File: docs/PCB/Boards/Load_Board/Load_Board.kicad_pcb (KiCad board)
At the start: 2 copper layers, 128 x 74.8 mm, 180 parts, among them J1 Conn_02x04_Odd_Even, J10 Conn_01x02_Pin, J11 Conn_01x02_Pin, J12 Conn_01x02_Pin, J13 Conn_01x02_Pin, J14 Conn_01x02_Pin, J15 Conn_01x02_Pin, J16 Conn_01x02_Pin, J17 Conn_01x01_Pin, J18 Conn_01x01_Pin, J19 Conn_01x01_Pin, J2 Conn_02x04_Odd_Even, J20 Conn_01x01_Pin, J21 Conn_01x01_Pin, J22 Conn_01x01_Pin, J23 Conn_01x01_Pin, J24 Conn_01x01_Pin, J25 Conn_01x01_Pin, J26 Conn_01x01_Pin, J27 Conn_01x01_Pin, J28 Conn_01x01_Pin, J29 Conn_01x01_Pin, J3 Conn_01x06_Pin, J30 Conn_01x01_Pin, J31 Conn_01x01_Pin, J32 Conn_01x01_Pin, J33 Conn_01x01_Pin, J34 Conn_01x01_Pin, J35 Conn_01x01_Pin, J36 Conn_01x01_Pin, J37 Conn_01x01_Pin, J38 Conn_01x01_Pin, J39 Conn_01x01_Pin, J4 Conn_01x06_Pin, J40 Conn_01x01_Pin, J41 Conn_01x01_Pin, J42 Conn_01x01_Pin, J43 Conn_01x01_Pin, J44 Conn_01x01_Pin, J45 Conn_01x01_Pin, J46 Conn_01x01_Pin, J47 Conn_01x01_Pin, J48 Conn_01x01_Pin, J49 Conn_01x01_Pin, J5 Conn_01x02_Pin, J50 Conn_01x01_Pin, J51 Conn_01x01_Pin, J52 Conn_01x01_Pin, J53 Conn_01x01_Pin, J54 Conn_01x01_Pin, J55 Conn_01x01_Pin, J56 Conn_01x01_Pin, J57 Conn_01x01_Pin, J58 Conn_01x01_Pin, J59 Conn_01x01_Pin, J6 Conn_01x02_Pin, J60 Conn_01x01_Pin, J61 Conn_01x01_Pin, J62 Conn_01x01_Pin, J63 Conn_01x01_Pin, J64 Conn_01x01_Pin, J65 Conn_01x01_Pin, J66 Conn_01x01_Pin, J67 Conn_01x01_Pin, J68 Conn_01x01_Pin, J69 Conn_01x01_Pin, J7 Conn_01x02_Pin, J70 Conn_01x01_Pin, J71 Conn_01x01_Pin, J72 Conn_01x01_Pin, J73 Conn_01x01_Pin, J74 Conn_01x01_Pin, J75 Conn_01x01_Pin, J76 Conn_01x01_Pin, J77 Conn_01x01_Pin, J78 Conn_01x01_Pin, J79 Conn_01x01_Pin, J8 Conn_01x02_Pin, J80 Conn_01x01_Pin, J81 Conn_01x01_Pin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

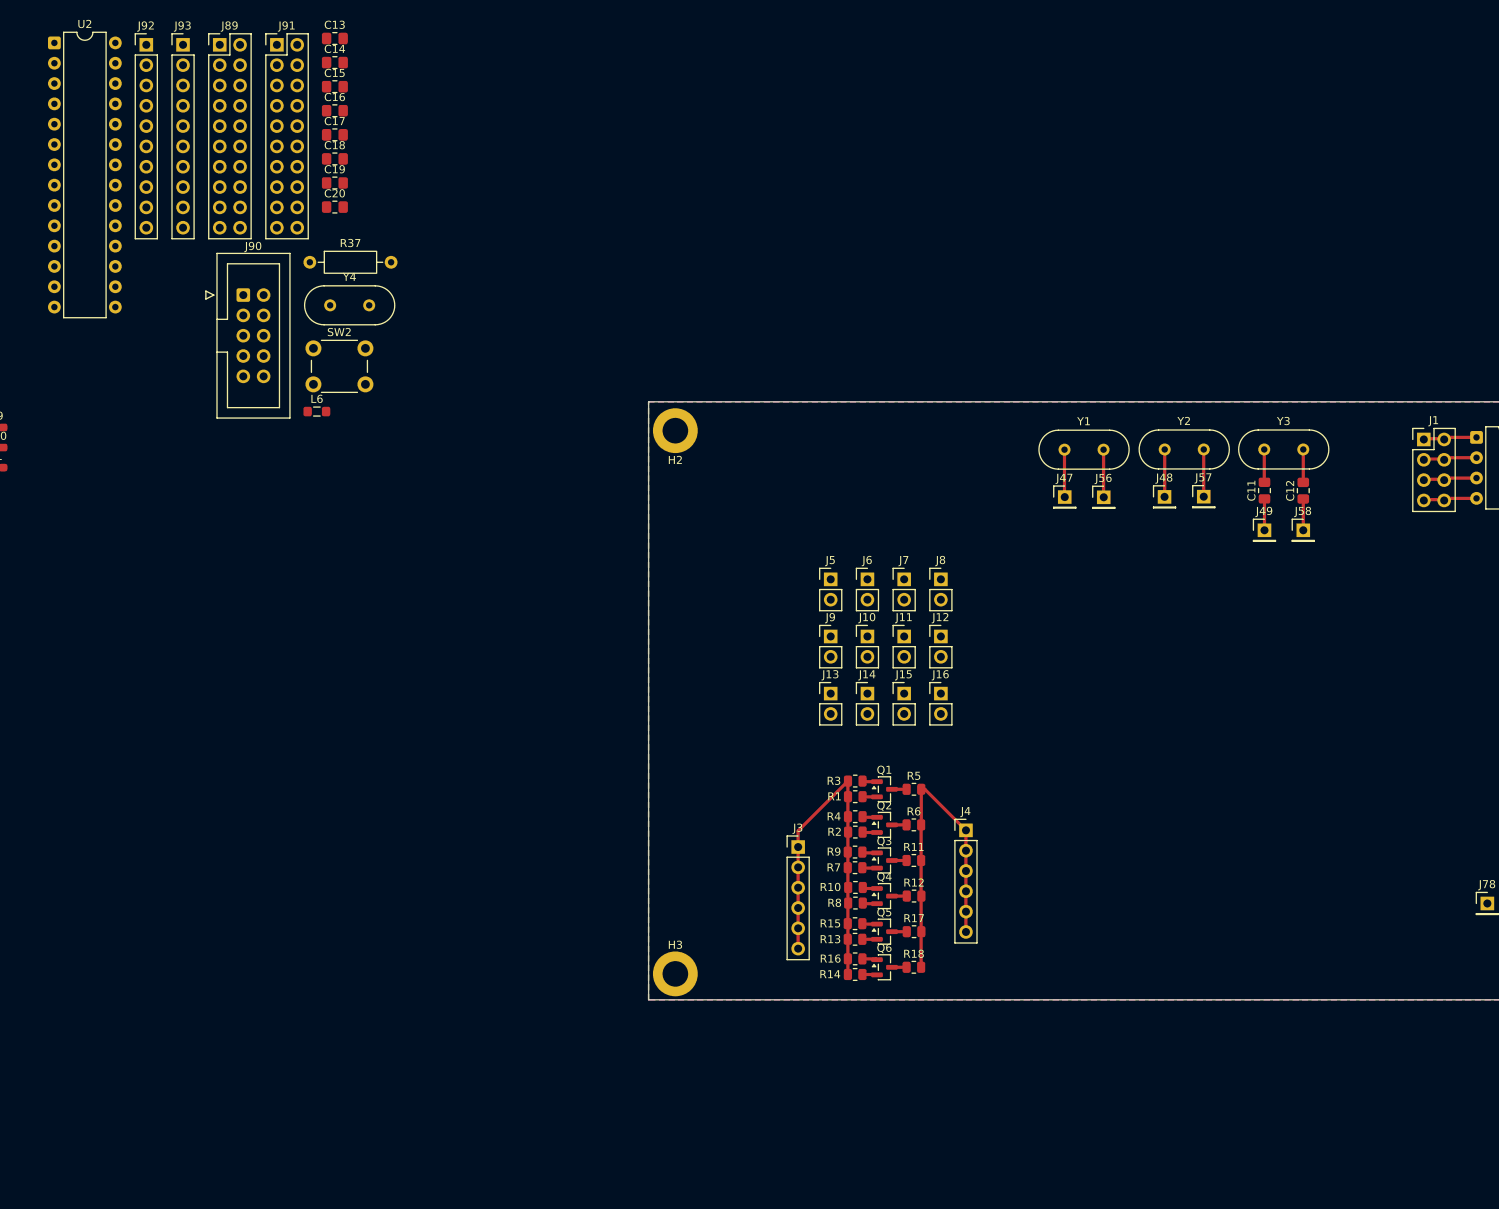
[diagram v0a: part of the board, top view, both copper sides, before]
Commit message: Load Board updated.
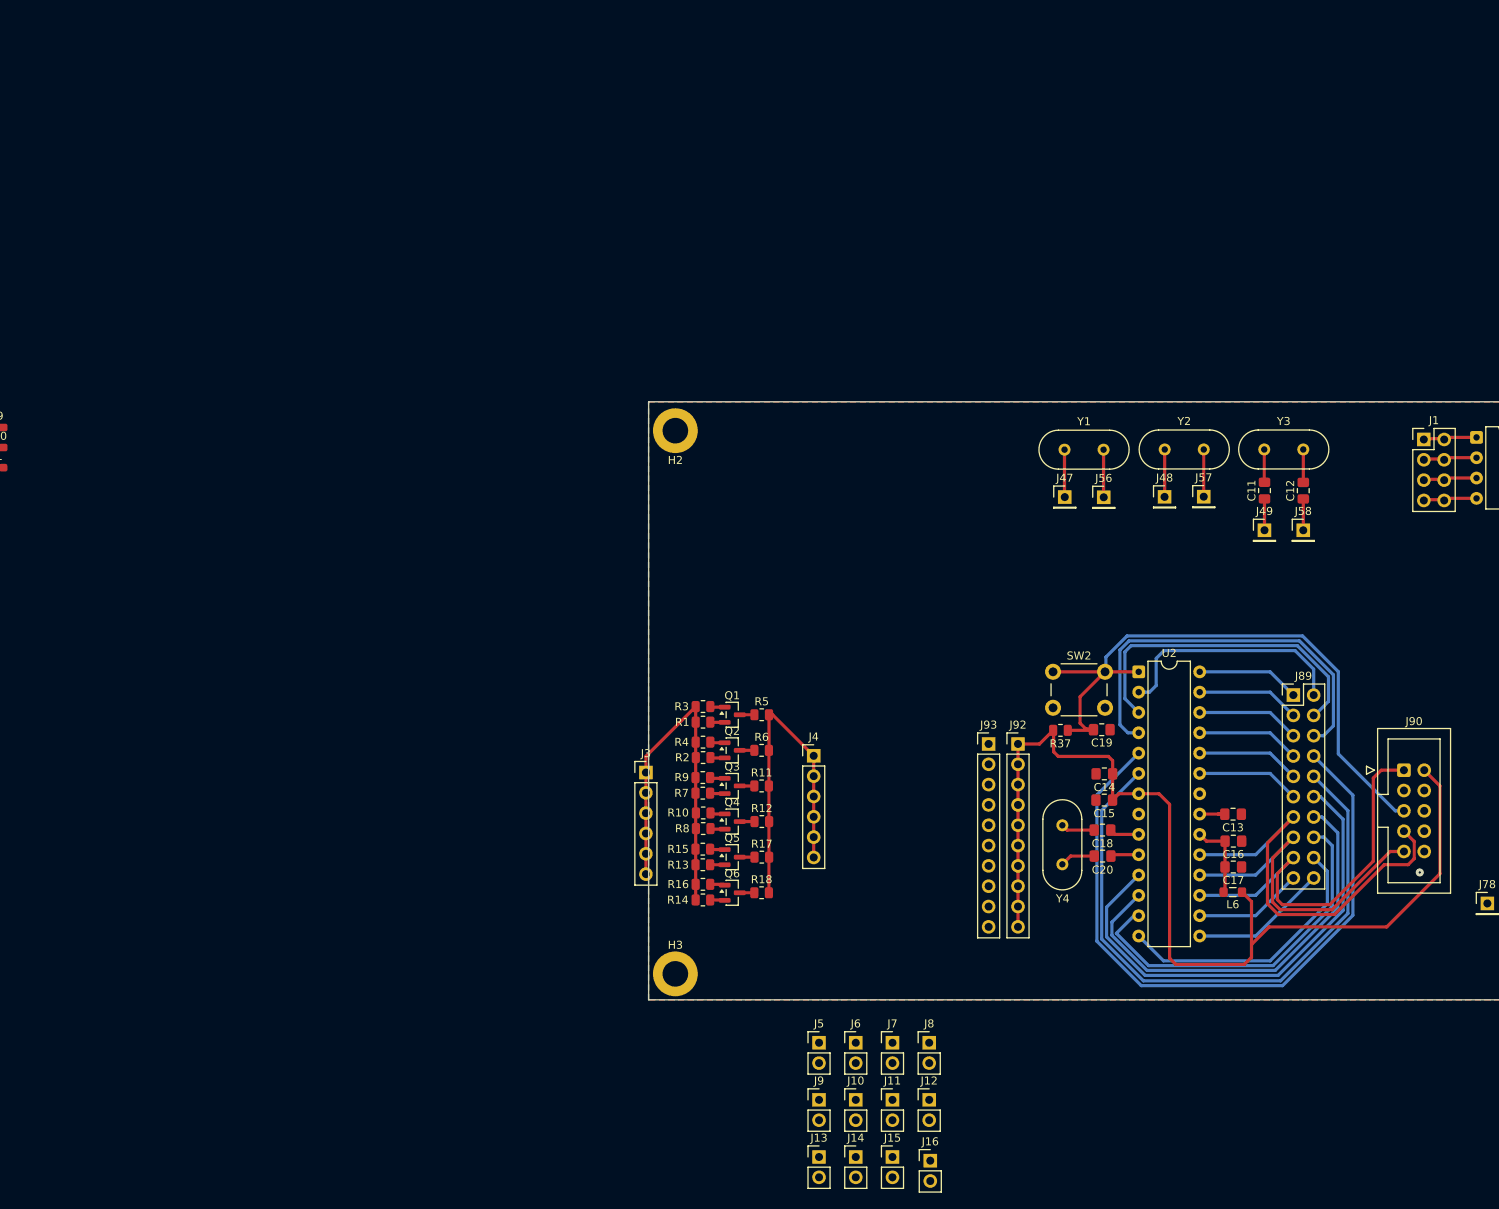
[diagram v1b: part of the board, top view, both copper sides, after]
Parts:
- removed J91: Conn_02x10_Odd_Even, Connector_PinHeader_2.54mm:PinHeader_2x10_P2.54mm_Vertical
- J90: value AVR-ISP-6 -> AVR-ISP-10
- R37: footprint Resistor_THT:R_Axial_DIN0207_L6.3mm_D2.5mm_P10.16mm_Horizontal -> Resistor_SMD:R_0805_2012Metric
- moved J89 156.9 mm to (202.3, 94.1)
- moved J90 156.8 mm to (216.1, 103.5)
- moved U2 156.7 mm to (183.0, 91.2)
- moved C13 148.3 mm to (194.8, 109.0), turned to 180 degrees
- moved C17 144.9 mm to (194.8, 115.6)
- moved C16 144.7 mm to (194.8, 112.4)
- moved J92 139.7 mm to (167.9, 100.2)
- moved J93 133.3 mm to (164.2, 100.2)
- moved C15 131.2 mm to (178.7, 107.2)
- moved C14 131.0 mm to (178.7, 104.0)
- moved L6 129.3 mm to (194.7, 118.7), turned to 180 degrees
- moved C18 127.5 mm to (178.4, 111.0), turned to 180 degrees
- moved C20 125.7 mm to (178.4, 114.2)
- moved C19 117.7 mm to (178.3, 98.4)
- moved Y4 112.3 mm to (173.4, 110.4), turned to -90 degrees
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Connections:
- J89 pad 1: PB0 -> PC5
- J89 pad 10: PD2 -> PD4
- J89 pad 11: PB5 -> PC0
- J89 pad 12: PD3 -> PD5
- J89 pad 13: PC0 -> PB5
- J89 pad 14: PD4 -> PD6
- J89 pad 15: PC1 -> PB4
- J89 pad 16: PD5 -> PD7
- J89 pad 17: PC2 -> PB3
- J89 pad 18: PD6 -> PB0
- J89 pad 19: PC3 -> PB2
- J89 pad 2: PC4 -> PD0
- J89 pad 20: PD7 -> PB1
- J89 pad 3: PB1 -> PC4
- J89 pad 4: PC5 -> PD1
- J89 pad 5: PB2 -> PC3
- J89 pad 6: PD0 -> PD2
- J89 pad 7: PB3 -> PC2
- J89 pad 8: PD1 -> PD3
- J89 pad 9: PB4 -> PC1
- J90 pad 1: PB4 -> PB3
- J90 pad 10: (no net) -> GND
- J90 pad 3: PB5 -> unconnected-(J90-NC-Pad3)
- J90 pad 4: PB3 -> GND
- J90 pad 7: (no net) -> PB5
- J90 pad 8: (no net) -> GND
- J90 pad 9: (no net) -> PB4
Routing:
- net 5V: track 0.00 -> 131.2 mm
- net PD3: track 0.00 -> 85.6 mm
- net RESET: track 0.00 -> 79.2 mm
- net PD4: track 0.00 -> 78.0 mm
- net PD5: track 0.00 -> 60.6 mm
- net PD6: track 0.00 -> 52.9 mm
- net PB5: track 0.00 -> 51.6 mm
- net PD2: track 0.00 -> 50.4 mm
- net PB3: track 0.00 -> 48.9 mm
- net PD7: track 0.00 -> 45.8 mm
- net PB4: track 0.00 -> 42.7 mm
- net PD1: track 0.00 -> 41.3 mm
- net PB0: track 0.00 -> 34.3 mm
- net PD0: track 0.00 -> 31.0 mm
- net PB1: track 0.00 -> 17.3 mm
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
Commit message: Load board and ATMega Board added
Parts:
- removed C13, C14, C16, C19: 100nF, Capacitor_SMD:C_0805_2012Metric_Pad1.18x1.45mm_HandSolder
- removed C15, C17: 1uF, Capacitor_SMD:C_0805_2012Metric_Pad1.18x1.45mm_HandSolder
- removed C18, C20: 22pF, Capacitor_SMD:C_0805_2012Metric_Pad1.18x1.45mm_HandSolder
- removed J17, J18, J19, J20, J39, J40, J41, J42, J43, J44, J45, J46, J47, J48, J49, J50, J51, J52, J53, J54, J55, J56, J57, J58, J59, J60, J61, J62, J63, J64, J65, J66, J67, J68, J69, J70, J71, J72, J73, J74, J75, J76, J77, J78, J79, J80, J81, J82, J83, J84, J85, J86, J87, J88: Conn_01x01_Pin, Connector_PinHeader_2.54mm:PinHeader_1x01_P2.54mm_Vertical
- removed J89: Conn_02x10_Odd_Even, Connector_PinHeader_2.54mm:PinHeader_2x10_P2.54mm_Vertical
- removed J90: AVR-ISP-10, Connector_IDC:IDC-Header_2x05_P2.54mm_Vertical
- removed J92, J93: Conn_01x10_Pin, Connector_PinHeader_2.54mm:PinHeader_1x10_P2.54mm_Vertical
- removed L6: 600 Ω@100 MHz, Inductor_SMD:L_0805_2012Metric_Pad1.05x1.20mm_HandSolder
- removed R37: 1K, Resistor_SMD:R_0805_2012Metric
- removed SW2: Tact Switch 6x6mm / 13mm, Button_Switch_THT:SW_PUSH_6mm
- removed U2: ATmega328P-P, Package_DIP:DIP-28_W7.62mm
- removed Y4: Crystal, Crystal:Crystal_HC49-4H_Vertical
- J10: value Conn_01x02_Pin -> LVL_OUT_3; footprint Connector_PinHeader_2.54mm:PinHeader_1x02_P2.54mm_Vertical -> Connector_PinHeader_2.54mm:PinHeader_1x01_P2.54mm_Vertical
- J11: value Conn_01x02_Pin -> LVL_IN_4; footprint Connector_PinHeader_2.54mm:PinHeader_1x02_P2.54mm_Vertical -> Connector_PinHeader_2.54mm:PinHeader_1x01_P2.54mm_Vertical
- J12: value Conn_01x02_Pin -> LVL_OUT_4; footprint Connector_PinHeader_2.54mm:PinHeader_1x02_P2.54mm_Vertical -> Connector_PinHeader_2.54mm:PinHeader_1x01_P2.54mm_Vertical
- J13: value Conn_01x02_Pin -> LVL_IN_6; footprint Connector_PinHeader_2.54mm:PinHeader_1x02_P2.54mm_Vertical -> Connector_PinHeader_2.54mm:PinHeader_1x01_P2.54mm_Vertical
- J14: value Conn_01x02_Pin -> LVL_OUT_6; footprint Connector_PinHeader_2.54mm:PinHeader_1x02_P2.54mm_Vertical -> Connector_PinHeader_2.54mm:PinHeader_1x01_P2.54mm_Vertical
- J15: value Conn_01x02_Pin -> LVL_IN_5; footprint Connector_PinHeader_2.54mm:PinHeader_1x02_P2.54mm_Vertical -> Connector_PinHeader_2.54mm:PinHeader_1x01_P2.54mm_Vertical
- J16: value Conn_01x02_Pin -> LVL_OUT_5; footprint Connector_PinHeader_2.54mm:PinHeader_1x02_P2.54mm_Vertical -> Connector_PinHeader_2.54mm:PinHeader_1x01_P2.54mm_Vertical
- J21: value Conn_01x01_Pin -> R_IN; footprint Connector_PinHeader_2.54mm:PinHeader_1x01_P2.54mm_Vertical -> Connector_PinHeader_2.54mm:PinHeader_1x09_P2.54mm_Vertical
- J22: value Conn_01x01_Pin -> R_OUT; footprint Connector_PinHeader_2.54mm:PinHeader_1x01_P2.54mm_Vertical -> Connector_PinHeader_2.54mm:PinHeader_1x09_P2.54mm_Vertical
- J23: value Conn_01x01_Pin -> SW_IN
- J24: value Conn_01x01_Pin -> SW_OUT
- J25: value Conn_01x01_Pin -> Divider_1; footprint Connector_PinHeader_2.54mm:PinHeader_1x01_P2.54mm_Vertical -> Connector_PinHeader_2.54mm:PinHeader_1x03_P2.54mm_Vertical
- J26: value Conn_01x01_Pin -> Divider_2; footprint Connector_PinHeader_2.54mm:PinHeader_1x01_P2.54mm_Vertical -> Connector_PinHeader_2.54mm:PinHeader_1x03_P2.54mm_Vertical
- J27: value Conn_01x01_Pin -> BZ_IN
- J28: value Conn_01x01_Pin -> BZ_OUT
- J29: value Conn_01x01_Pin -> LED_IN; footprint Connector_PinHeader_2.54mm:PinHeader_1x01_P2.54mm_Vertical -> Connector_PinSocket_2.54mm:PinSocket_1x03_P2.54mm_Vertical
- J30: value Conn_01x01_Pin -> LED_OUT; footprint Connector_PinHeader_2.54mm:PinHeader_1x01_P2.54mm_Vertical -> Connector_PinSocket_2.54mm:PinSocket_1x03_P2.54mm_Vertical
- J31: value Conn_01x01_Pin -> CRYSTAL_IN; footprint Connector_PinHeader_2.54mm:PinHeader_1x01_P2.54mm_Vertical -> Connector_PinSocket_2.54mm:PinSocket_1x03_P2.54mm_Vertical
- J32: value Conn_01x01_Pin -> CRYSTAL_OUT; footprint Connector_PinHeader_2.54mm:PinHeader_1x01_P2.54mm_Vertical -> Connector_PinSocket_2.54mm:PinSocket_1x03_P2.54mm_Vertical
- J33: value Conn_01x01_Pin -> T_1; footprint Connector_PinHeader_2.54mm:PinHeader_1x01_P2.54mm_Vertical -> Connector_PinSocket_2.54mm:PinSocket_1x03_P2.54mm_Vertical
- J34: value Conn_01x01_Pin -> T_2; footprint Connector_PinHeader_2.54mm:PinHeader_1x01_P2.54mm_Vertical -> Connector_PinSocket_2.54mm:PinSocket_1x03_P2.54mm_Vertical
- J35: value Conn_01x01_Pin -> L_IN; footprint Connector_PinHeader_2.54mm:PinHeader_1x01_P2.54mm_Vertical -> Connector_PinHeader_2.54mm:PinHeader_1x05_P2.54mm_Vertical
- J36: value Conn_01x01_Pin -> L_OUT; footprint Connector_PinHeader_2.54mm:PinHeader_1x01_P2.54mm_Vertical -> Connector_PinHeader_2.54mm:PinHeader_1x05_P2.54mm_Vertical
- J37: value Conn_01x01_Pin -> C_IN; footprint Connector_PinHeader_2.54mm:PinHeader_1x01_P2.54mm_Vertical -> Connector_PinHeader_2.54mm:PinHeader_1x08_P2.54mm_Vertical
- J38: value Conn_01x01_Pin -> C_OUT; footprint Connector_PinHeader_2.54mm:PinHeader_1x01_P2.54mm_Vertical -> Connector_PinHeader_2.54mm:PinHeader_1x08_P2.54mm_Vertical
- J5: value Conn_01x02_Pin -> LVL_IN_2; footprint Connector_PinHeader_2.54mm:PinHeader_1x02_P2.54mm_Vertical -> Connector_PinHeader_2.54mm:PinHeader_1x01_P2.54mm_Vertical
- J6: value Conn_01x02_Pin -> LVL_OUT_2; footprint Connector_PinHeader_2.54mm:PinHeader_1x02_P2.54mm_Vertical -> Connector_PinHeader_2.54mm:PinHeader_1x01_P2.54mm_Vertical
- J7: value Conn_01x02_Pin -> LVL_IN_1; footprint Connector_PinHeader_2.54mm:PinHeader_1x02_P2.54mm_Vertical -> Connector_PinHeader_2.54mm:PinHeader_1x01_P2.54mm_Vertical
- J8: value Conn_01x02_Pin -> LVL_OUT_1; footprint Connector_PinHeader_2.54mm:PinHeader_1x02_P2.54mm_Vertical -> Connector_PinHeader_2.54mm:PinHeader_1x01_P2.54mm_Vertical
- J9: value Conn_01x02_Pin -> LVL_IN_3; footprint Connector_PinHeader_2.54mm:PinHeader_1x02_P2.54mm_Vertical -> Connector_PinHeader_2.54mm:PinHeader_1x01_P2.54mm_Vertical
- moved J26 221.6 mm to (191.0, 117.3)
- moved J25 215.6 mm to (181.8, 117.3)
- moved J34 210.2 mm to (188.9, 105.0), turned to 180 degrees
- moved J33 205.0 mm to (180.9, 105.0), turned to 180 degrees
- moved C2 202.7 mm to (186.7, 126.3)
- moved J28 202.3 mm to (191.5, 66.4)
- moved C1 195.3 mm to (177.5, 126.3)
- moved J24 194.3 mm to (178.1, 87.8)
- moved R22 194.2 mm to (186.8, 119.8)
- moved J23 194.2 mm to (178.1, 82.8)
- moved R21 194.1 mm to (186.8, 116.5), turned to 180 degrees
- moved R24 193.4 mm to (186.9, 123.0), turned to 180 degrees
- moved R20 187.6 mm to (177.7, 119.8)
- moved R19 187.4 mm to (177.6, 116.5), turned to 180 degrees
- moved J27 187.2 mm to (175.0, 66.4)
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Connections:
- C1 pad 2: GND -> Divider_GND_1
- C2 pad 2: GND -> Divider_GND_2
- J10 pad 1: COM_5V_4 -> COM_5V_3
- J11 pad 1: COM_3V3_3 -> COM_3V3_4
- J12 pad 1: COM_5V_3 -> COM_5V_4
- J21 pad 1: Load_L_IN_4 -> Load_R_IN_1
- J22 pad 1: Divider_IN_1 -> Load_R_OUT_1
- J23 pad 1: Divider_GND_1 -> SW_IN
- J24 pad 1: Divider_OUT_1 -> SW_OUT
- J25 pad 1: Load_LED_IN_1 -> Divider_IN_1
- J26 pad 1: Load_LED_IN_2 -> Divider_IN_2
- J27 pad 1: Load_LED_IN_3 -> BZ_IN
- J28 pad 1: Load_L_OUT_5 -> BZ_OUT
- J29 pad 1: Load_L_OUT_1 -> Load_LED_IN_1
- J30 pad 1: Load_L_OUT_2 -> Load_LED_OUT_1
- J31 pad 1: Load_L_OUT_3 -> Load_Crystal_IN_1
- J32 pad 1: Load_L_OUT_4 -> Load_Crystal_OUT_1
- J33 pad 1: Divider_IN_2 -> T1_1
- J34 pad 1: Divider_GND_2 -> T2_1
- J35 pad 1: Divider_OUT_2 -> Load_L_IN_1
- J36 pad 1: Load_LED_OUT_1 -> Load_L_OUT_1
- J37 pad 1: Load_LED_OUT_2 -> Load_C_IN_1
- J38 pad 1: Load_LED_OUT_3 -> Load_C_OUT_1
- J9 pad 1: COM_3V3_4 -> COM_3V3_3
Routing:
- net 5V: track 131.2 -> 0.00 mm
- net PD3: track 85.6 -> 0.00 mm
- net RESET: track 79.2 -> 0.00 mm
- net PD4: track 78.0 -> 0.00 mm
- net PD5: track 60.6 -> 0.00 mm
- net PD6: track 52.9 -> 0.00 mm
- net PB5: track 51.6 -> 0.00 mm
- net PD2: track 50.4 -> 0.00 mm
- net PB3: track 48.9 -> 0.00 mm
- net PD7: track 45.8 -> 0.00 mm
- net PB4: track 42.7 -> 0.00 mm
- net PD1: track 41.3 -> 0.00 mm
- net PB0: track 34.3 -> 0.00 mm
- net 3V3_IN: track 47.7 -> 79.0 mm
- net PD0: track 31.0 -> 0.00 mm
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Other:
- board size 128 x 74.8 mm -> 108.1 x 74.8 mm

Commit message: Hardware docs updated.
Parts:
- added J39: RV1, Connector_PinSocket_2.54mm:PinSocket_1x03_P2.54mm_Vertical, F.Cu at (171.2, 84.0)
- added J40: RV2, Connector_PinSocket_2.54mm:PinSocket_1x03_P2.54mm_Vertical, F.Cu at (181.2, 84.0)
- added J41: RV3, Connector_PinSocket_2.54mm:PinSocket_1x03_P2.54mm_Vertical, F.Cu at (191.2, 84.0)
- added RV1: R_Potentiometer, Potentiometer_THT:Potentiometer_Runtron_RM-065_Vertical, F.Cu at (171.4, 76.0)
- added RV2: R_Potentiometer, Potentiometer_THT:Potentiometer_Runtron_RM-065_Vertical, F.Cu at (181.3, 76.0)
- added RV3: R_Potentiometer, Potentiometer_THT:Potentiometer_Runtron_RM-065_Vertical, F.Cu at (191.2, 76.0)
- moved J23 44.6 mm to (203.8, 119.2)
- moved J24 44.6 mm to (203.8, 124.2)
- moved SW1 44.6 mm to (208.1, 118.9)
- moved R25 3.76 mm to (138.8, 59.9)
- moved R26 3.76 mm to (138.8, 63.1)
- moved R27 3.76 mm to (138.8, 66.3)
- moved R31 3.76 mm to (138.8, 69.5)
- moved R32 3.76 mm to (138.9, 72.8)
- moved R33 3.76 mm to (138.9, 76.0)
- moved BZ1 2.33 mm to (178.4, 64.3)
- moved J27 2.33 mm to (174.0, 64.3)
- moved J28 2.33 mm to (190.5, 64.3)
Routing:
- net RV3_3: track 0.00 -> 8.18 mm
- net RV1_1: track 0.00 -> 8.04 mm
- net RV2_1: track 0.00 -> 8.04 mm
- net RV1_3: track 0.00 -> 8.01 mm
- net RV2_3: track 0.00 -> 8.01 mm
- net RV3_1: track 0.00 -> 8.00 mm
- net Load_R_IN_5: track 4.62 -> 8.39 mm
- net Load_R_OUT_6: track 12.2 -> 8.43 mm
- net Load_R_IN_3: track 3.98 -> 7.74 mm
- net Load_R_IN_2: track 3.68 -> 7.44 mm
- net Load_R_IN_1: track 3.61 -> 7.37 mm
- net Load_R_OUT_2: track 11.2 -> 7.40 mm
- net Load_R_OUT_5: track 11.9 -> 8.14 mm
- net Load_R_OUT_4: track 11.7 -> 7.90 mm
- net Load_R_OUT_3: track 11.5 -> 7.70 mm
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
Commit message: Code review
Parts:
- moved C1 17.4 mm to (171.6, 109.9)
- moved J26 17.4 mm to (185.0, 100.9)
- moved R19 17.4 mm to (171.7, 100.1)
- moved R23 17.4 mm to (171.7, 106.7)
- moved R24 17.4 mm to (180.9, 106.6)
- moved C2 17.4 mm to (180.8, 109.9)
- moved J25 17.4 mm to (175.9, 100.9)
- moved R20 17.4 mm to (171.7, 103.4)
- moved R21 17.4 mm to (180.9, 100.1)
- moved R22 17.4 mm to (180.9, 103.4)
- moved J23 17.4 mm to (188.3, 111.3)
- moved J24 17.4 mm to (188.3, 116.2)
- moved SW1 17.4 mm to (192.6, 111.0)
- moved J33 13.1 mm to (174.0, 93.9)
- moved J34 13.1 mm to (182.0, 93.9)
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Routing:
- net Divider_GND_1: track 11.2 -> 10.6 mm
- net Divider_IN_1: track 4.32 -> 3.67 mm
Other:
- board size 108.1 x 74.8 mm -> 106.6 x 64.8 mm
